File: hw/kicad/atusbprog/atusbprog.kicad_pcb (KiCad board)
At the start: 2 copper layers, 91.4 x 61 mm, 30 parts, among them J1 SMH-110-02-L-D, J2 Conn_01x04, J3 Conn_01x08, J4 Conn_01x08, J5 Conn_01x08, SW1 SW_Push, SW2 SW_Push, U1 SN74HCT125, U2 AT89S52-24PU, Y1 24 MHz

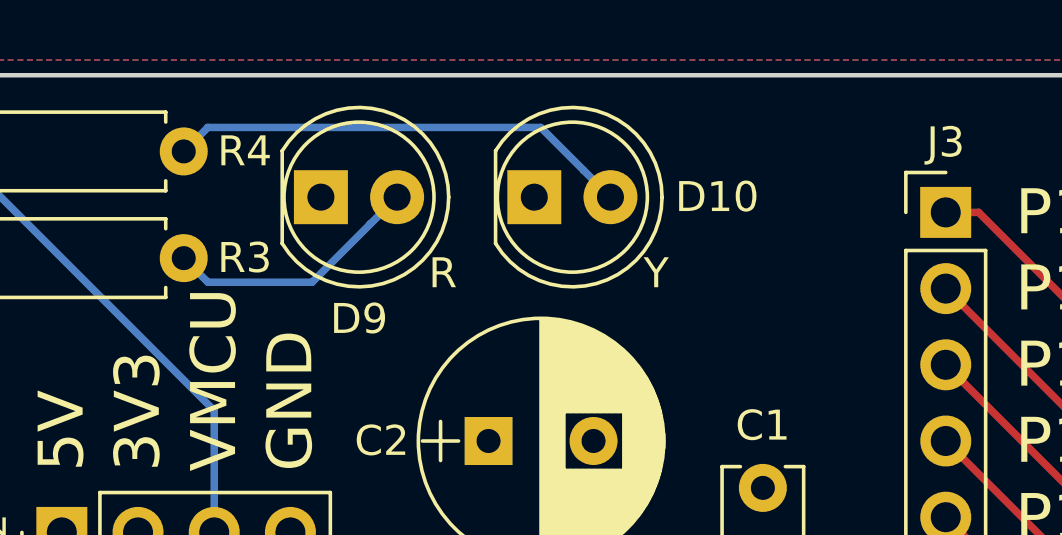
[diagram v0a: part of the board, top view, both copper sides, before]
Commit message: Move power LEDs
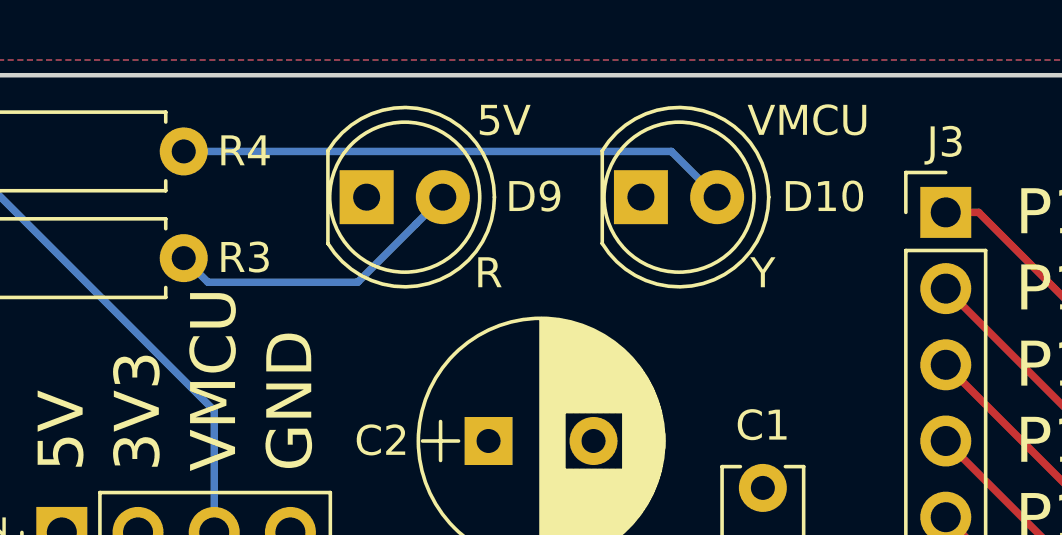
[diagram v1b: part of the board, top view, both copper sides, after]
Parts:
- moved D10 3.56 mm to (130.0, 70.1)
- moved D9 1.52 mm to (120.9, 70.1)
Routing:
- net Net-(D10-Pad2): track 15.5 -> 18.4 mm
- net Net-(D9-Pad2): track 8.62 -> 10.1 mm
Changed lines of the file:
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@@
   (general
     (thickness 1.6002)
-    (drawings 48)
-    (tracks 226)
+    (drawings 50)
+    (tracks 224)
     (zones 0)
     (modules 30)
@@
   )
   (module LEDs:LED_D5.0mm (layer F.Cu)
-    (at 126.492 70.104)
+    (at 130.048 70.104)
     (descr "LED, diameter 5.0mm, 2 pins, http://cdn-reichelt.de/documents/datenblatt/A500/LL-504BC2E-009.pdf")
     (tags "LED diameter 5.0mm 2 pins")
@@
   )
   (module LEDs:LED_D5.0mm (layer F.Cu)
-    (at 119.38 70.104)
+    (at 120.904 70.104)
     (descr "LED, diameter 5.0mm, 2 pins, http://cdn-reichelt.de/documents/datenblatt/A500/LL-504BC2E-009.pdf")
     (tags "LED diameter 5.0mm 2 pins")
-    (fp_text reference D9 (at 1.27 4.064) (layer F.SilkS)
+    (fp_text reference D9 (at 5.588 0) (layer F.SilkS)
       (effects (font (size 1 1) (thickness 0.15)))
     )
@@
     )
   )
-  (gr_text Y (at 130.556 72.644) (layer F.SilkS)
+  (gr_text 5V (at 125.476 67.564) (layer F.SilkS)
     (effects (font (size 1 1) (thickness 0.15)))
   )
-  (gr_text R (at 123.444 72.644) (layer F.SilkS)
+  (gr_text VMCU (at 135.636 67.564) (layer F.SilkS)
+    (effects (font (size 1 1) (thickness 0.15)))
+  )
+  (gr_text Y (at 134.112 72.644) (layer F.SilkS)
+    (effects (font (size 1 1) (thickness 0.15)))
+  )
+  (gr_text R (at 124.968 72.644) (layer F.SilkS)
     (effects (font (size 1 1) (thickness 0.15)))
   )
@@
   (segment (start 115.824 77.216) (end 107.188 68.58) (width 0.25) (layer B.Cu) (net 66))
   (segment (start 115.824 81.28) (end 115.824 77.216) (width 0.25) (layer B.Cu) (net 66))
-  (segment (start 121.020001 71.003999) (end 121.92 70.104) (width 0.25) (layer B.Cu) (net 67))
-  (segment (start 119.088001 72.935999) (end 121.020001 71.003999) (width 0.25) (layer B.Cu) (net 67))
-  (segment (start 115.607999 72.935999) (end 119.088001 72.935999) (width 0.25) (layer B.Cu) (net 67))
+  (segment (start 122.544001 71.003999) (end 123.444 70.104) (width 0.25) (layer B.Cu) (net 67))
+  (segment (start 115.607999 72.935999) (end 120.612001 72.935999) (width 0.25) (layer B.Cu) (net 67))
+  (segment (start 120.612001 72.935999) (end 122.544001 71.003999) (width 0.25) (layer B.Cu) (net 67))
   (segment (start 114.808 72.136) (end 115.607999 72.935999) (width 0.25) (layer B.Cu) (net 67))
-  (segment (start 128.132001 69.204001) (end 129.032 70.104) (width 0.25) (layer B.Cu) (net 68))
-  (segment (start 126.708001 67.780001) (end 128.132001 69.204001) (width 0.25) (layer B.Cu) (net 68))
-  (segment (start 115.607999 67.780001) (end 126.708001 67.780001) (width 0.25) (layer B.Cu) (net 68))
-  (segment (start 114.808 68.58) (end 115.607999 67.780001) (width 0.25) (layer B.Cu) (net 68))
+  (segment (start 131.064 68.58) (end 132.588 70.104) (width 0.25) (layer B.Cu) (net 68))
+  (segment (start 114.808 68.58) (end 131.064 68.58) (width 0.25) (layer B.Cu) (net 68))
   (zone (net 3) (net_name +5V) (layer B.Cu) (hatch edge 0.508)
     (connect_pads (clearance 0.508))
